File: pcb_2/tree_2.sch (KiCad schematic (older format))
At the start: 28 parts, among them J1 CONN_01x08, J2 CONN_01x08, X1 Silk_art

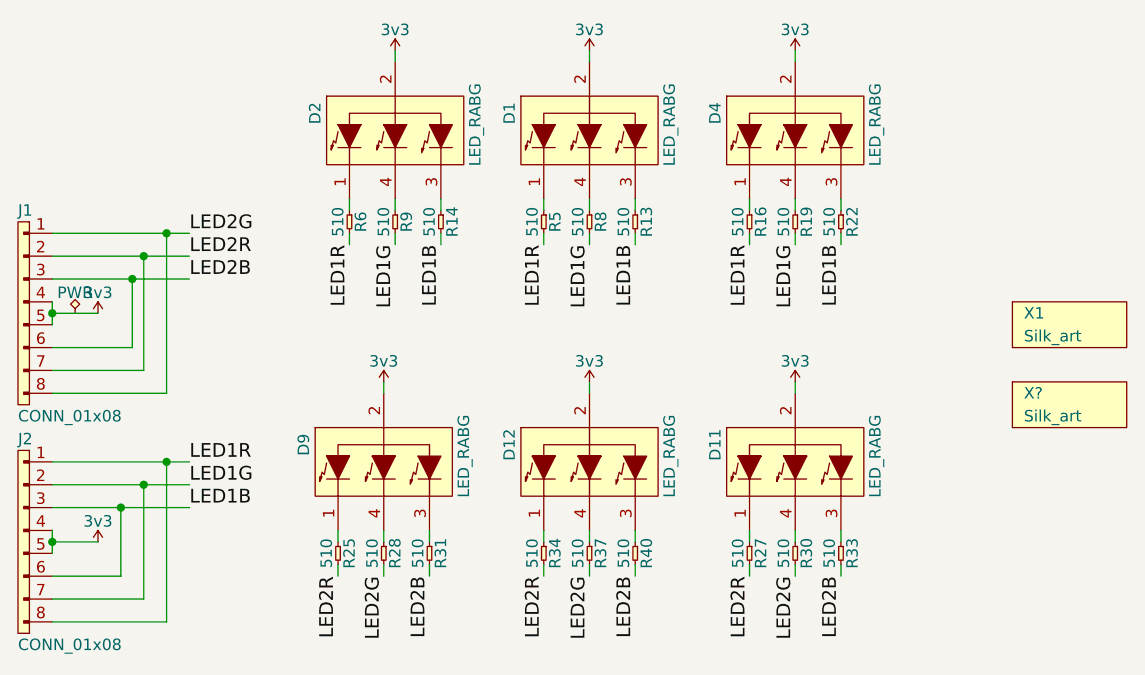
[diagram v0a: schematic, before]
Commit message: Fix circuit to account for LED currents: change resistor values, upgrade LDO regulator, use transistor array
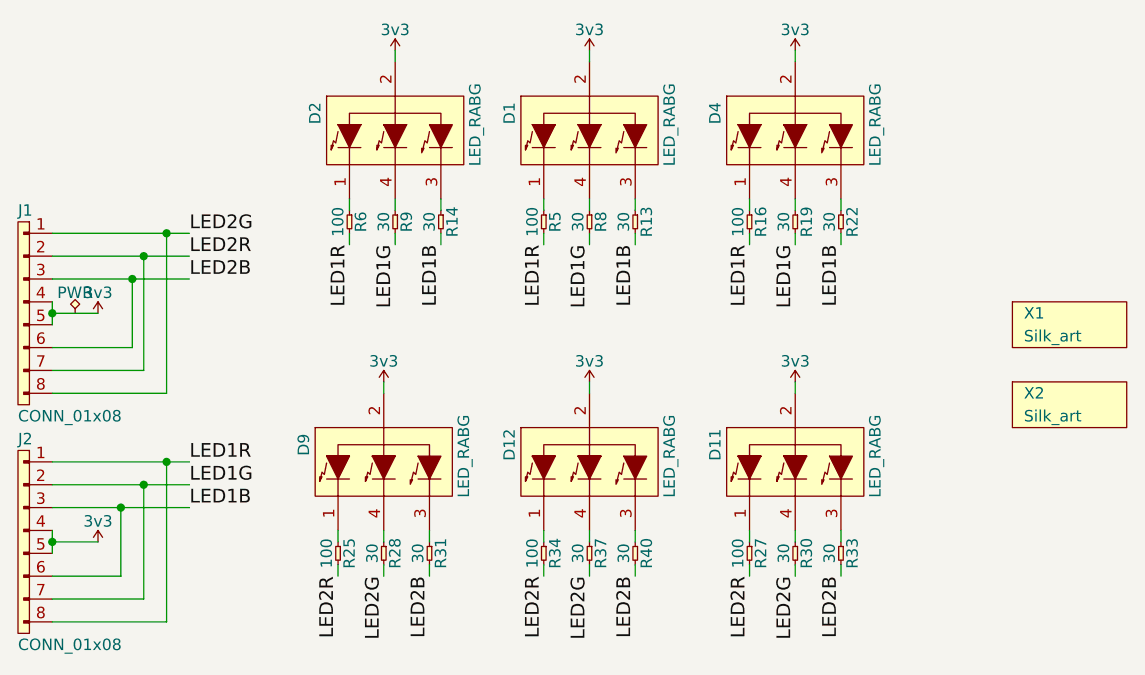
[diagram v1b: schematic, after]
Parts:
- R13, R14, R19, R22, R28, R30, R31, R33, R37, R40, R8, R9: value 510 -> 30; Farnell 9333312 -> 9333029
- R16, R25, R27, R34, R5, R6: value 510 -> 100; Farnell 9333312 -> 9332375
- gave numbers to parts that had none: 1
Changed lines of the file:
@@
 P 5750 3250
 F 0 "R31" H 5800 3300 50  0000 C CNN
-F 1 "510" H 5800 3200 50  0000 C CNN
+F 1 "30" H 5800 3200 50  0000 C CNN
 F 2 "agg:0805" H 5750 3250 50  0001 C CNN
 F 3 "" H 5750 3250 50  0001 C CNN
 F 4 "Value" H 5750 3250 60  0001 C CNN "Digikey"
-F 5 "9333312" H 5750 3250 60  0001 C CNN "Farnell"
+F 5 "9333029" H 5750 3250 60  0001 C CNN "Farnell"
 F 6 "Value" H 5750 3250 60  0001 C CNN "Fieldname"
 	1    5750 3250
@@
 P 5550 3250
 F 0 "R28" H 5600 3300 50  0000 C CNN
-F 1 "510" H 5600 3200 50  0000 C CNN
+F 1 "30" H 5600 3200 50  0000 C CNN
 F 2 "agg:0805" H 5550 3250 50  0001 C CNN
 F 3 "" H 5550 3250 50  0001 C CNN
 F 4 "Value" H 5550 3250 60  0001 C CNN "Digikey"
-F 5 "9333312" H 5550 3250 60  0001 C CNN "Farnell"
+F 5 "9333029" H 5550 3250 60  0001 C CNN "Farnell"
 F 6 "Value" H 5550 3250 60  0001 C CNN "Fieldname"
 	1    5550 3250
@@
 P 5350 3250
 F 0 "R25" H 5400 3300 50  0000 C CNN
-F 1 "510" H 5400 3200 50  0000 C CNN
+F 1 "100" H 5400 3200 50  0000 C CNN
 F 2 "agg:0805" H 5350 3250 50  0001 C CNN
 F 3 "" H 5350 3250 50  0001 C CNN
 F 4 "Value" H 5350 3250 60  0001 C CNN "Digikey"
-F 5 "9333312" H 5350 3250 60  0001 C CNN "Farnell"
+F 5 "9332375" H 5350 3250 60  0001 C CNN "Farnell"
 F 6 "Value" H 5350 3250 60  0001 C CNN "Fieldname"
 	1    5350 3250
@@
 P 7550 3250
 F 0 "R33" H 7600 3300 50  0000 C CNN
-F 1 "510" H 7600 3200 50  0000 C CNN
+F 1 "30" H 7600 3200 50  0000 C CNN
 F 2 "agg:0805" H 7550 3250 50  0001 C CNN
 F 3 "" H 7550 3250 50  0001 C CNN
 F 4 "Value" H 7550 3250 60  0001 C CNN "Digikey"
-F 5 "9333312" H 7550 3250 60  0001 C CNN "Farnell"
+F 5 "9333029" H 7550 3250 60  0001 C CNN "Farnell"
 F 6 "Value" H 7550 3250 60  0001 C CNN "Fieldname"
 	1    7550 3250
@@
 P 7350 3250
 F 0 "R30" H 7400 3300 50  0000 C CNN
-F 1 "510" H 7400 3200 50  0000 C CNN
+F 1 "30" H 7400 3200 50  0000 C CNN
 F 2 "agg:0805" H 7350 3250 50  0001 C CNN
 F 3 "" H 7350 3250 50  0001 C CNN
 F 4 "Value" H 7350 3250 60  0001 C CNN "Digikey"
-F 5 "9333312" H 7350 3250 60  0001 C CNN "Farnell"
+F 5 "9333029" H 7350 3250 60  0001 C CNN "Farnell"
 F 6 "Value" H 7350 3250 60  0001 C CNN "Fieldname"
 	1    7350 3250
@@
 P 7150 3250
 F 0 "R27" H 7200 3300 50  0000 C CNN
-F 1 "510" H 7200 3200 50  0000 C CNN
+F 1 "100" H 7200 3200 50  0000 C CNN
 F 2 "agg:0805" H 7150 3250 50  0001 C CNN
 F 3 "" H 7150 3250 50  0001 C CNN
 F 4 "Value" H 7150 3250 60  0001 C CNN "Digikey"
-F 5 "9333312" H 7150 3250 60  0001 C CNN "Farnell"
+F 5 "9332375" H 7150 3250 60  0001 C CNN "Farnell"
 F 6 "Value" H 7150 3250 60  0001 C CNN "Fieldname"
 	1    7150 3250
@@
 P 6650 3250
 F 0 "R40" H 6700 3300 50  0000 C CNN
-F 1 "510" H 6700 3200 50  0000 C CNN
+F 1 "30" H 6700 3200 50  0000 C CNN
 F 2 "agg:0805" H 6650 3250 50  0001 C CNN
 F 3 "" H 6650 3250 50  0001 C CNN
 F 4 "Value" H 6650 3250 60  0001 C CNN "Digikey"
-F 5 "9333312" H 6650 3250 60  0001 C CNN "Farnell"
+F 5 "9333029" H 6650 3250 60  0001 C CNN "Farnell"
 F 6 "Value" H 6650 3250 60  0001 C CNN "Fieldname"
 	1    6650 3250
@@
 P 6450 3250
 F 0 "R37" H 6500 3300 50  0000 C CNN
-F 1 "510" H 6500 3200 50  0000 C CNN
+F 1 "30" H 6500 3200 50  0000 C CNN
 F 2 "agg:0805" H 6450 3250 50  0001 C CNN
 F 3 "" H 6450 3250 50  0001 C CNN
 F 4 "Value" H 6450 3250 60  0001 C CNN "Digikey"
-F 5 "9333312" H 6450 3250 60  0001 C CNN "Farnell"
+F 5 "9333029" H 6450 3250 60  0001 C CNN "Farnell"
 F 6 "Value" H 6450 3250 60  0001 C CNN "Fieldname"
 	1    6450 3250
@@
 P 6250 3250
 F 0 "R34" H 6300 3300 50  0000 C CNN
-F 1 "510" H 6300 3200 50  0000 C CNN
+F 1 "100" H 6300 3200 50  0000 C CNN
 F 2 "agg:0805" H 6250 3250 50  0001 C CNN
 F 3 "" H 6250 3250 50  0001 C CNN
 F 4 "Value" H 6250 3250 60  0001 C CNN "Digikey"
-F 5 "9333312" H 6250 3250 60  0001 C CNN "Farnell"
+F 5 "9332375" H 6250 3250 60  0001 C CNN "Farnell"
 F 6 "Value" H 6250 3250 60  0001 C CNN "Fieldname"
 	1    6250 3250
@@
 P 7150 1800
 F 0 "R16" H 7200 1850 50  0000 C CNN
-F 1 "510" H 7200 1750 50  0000 C CNN
+F 1 "100" H 7200 1750 50  0000 C CNN
 F 2 "agg:0805" H 7150 1800 50  0001 C CNN
 F 3 "" H 7150 1800 50  0001 C CNN
 F 4 "Value" H 7150 1800 60  0001 C CNN "Digikey"
-F 5 "9333312" H 7150 1800 60  0001 C CNN "Farnell"
+F 5 "9332375" H 7150 1800 60  0001 C CNN "Farnell"
 F 6 "Value" H 7150 1800 60  0001 C CNN "Fieldname"
 	1    7150 1800
@@
 P 7350 1800
 F 0 "R19" H 7400 1850 50  0000 C CNN
-F 1 "510" H 7400 1750 50  0000 C CNN
+F 1 "30" H 7400 1750 50  0000 C CNN
 F 2 "agg:0805" H 7350 1800 50  0001 C CNN
 F 3 "" H 7350 1800 50  0001 C CNN
 F 4 "Value" H 7350 1800 60  0001 C CNN "Digikey"
-F 5 "9333312" H 7350 1800 60  0001 C CNN "Farnell"
+F 5 "9333029" H 7350 1800 60  0001 C CNN "Farnell"
 F 6 "Value" H 7350 1800 60  0001 C CNN "Fieldname"
 	1    7350 1800
@@
 P 7550 1800
 F 0 "R22" H 7600 1850 50  0000 C CNN
-F 1 "510" H 7600 1750 50  0000 C CNN
+F 1 "30" H 7600 1750 50  0000 C CNN
 F 2 "agg:0805" H 7550 1800 50  0001 C CNN
 F 3 "" H 7550 1800 50  0001 C CNN
 F 4 "Value" H 7550 1800 60  0001 C CNN "Digikey"
-F 5 "9333312" H 7550 1800 60  0001 C CNN "Farnell"
+F 5 "9333029" H 7550 1800 60  0001 C CNN "Farnell"
 F 6 "Value" H 7550 1800 60  0001 C CNN "Fieldname"
 	1    7550 1800
@@
 P 5400 1800
 F 0 "R6" H 5450 1850 50  0000 C CNN
-F 1 "510" H 5450 1750 50  0000 C CNN
+F 1 "100" H 5450 1750 50  0000 C CNN
 F 2 "agg:0805" H 5400 1800 50  0001 C CNN
 F 3 "" H 5400 1800 50  0001 C CNN
 F 4 "Value" H 5400 1800 60  0001 C CNN "Digikey"
-F 5 "9333312" H 5400 1800 60  0001 C CNN "Farnell"
+F 5 "9332375" H 5400 1800 60  0001 C CNN "Farnell"
 F 6 "Value" H 5400 1800 60  0001 C CNN "Fieldname"
 	1    5400 1800
@@
 P 5600 1800
 F 0 "R9" H 5650 1850 50  0000 C CNN
-F 1 "510" H 5650 1750 50  0000 C CNN
+F 1 "30" H 5650 1750 50  0000 C CNN
 F 2 "agg:0805" H 5600 1800 50  0001 C CNN
 F 3 "" H 5600 1800 50  0001 C CNN
 F 4 "Value" H 5600 1800 60  0001 C CNN "Digikey"
-F 5 "9333312" H 5600 1800 60  0001 C CNN "Farnell"
+F 5 "9333029" H 5600 1800 60  0001 C CNN "Farnell"
 F 6 "Value" H 5600 1800 60  0001 C CNN "Fieldname"
 	1    5600 1800
@@
 P 5800 1800
 F 0 "R14" H 5850 1850 50  0000 C CNN
-F 1 "510" H 5850 1750 50  0000 C CNN
+F 1 "30" H 5850 1750 50  0000 C CNN
 F 2 "agg:0805" H 5800 1800 50  0001 C CNN
 F 3 "" H 5800 1800 50  0001 C CNN
 F 4 "Value" H 5800 1800 60  0001 C CNN "Digikey"
-F 5 "9333312" H 5800 1800 60  0001 C CNN "Farnell"
+F 5 "9333029" H 5800 1800 60  0001 C CNN "Farnell"
 F 6 "Value" H 5800 1800 60  0001 C CNN "Fieldname"
 	1    5800 1800
@@
 P 6250 1800
 F 0 "R5" H 6300 1850 50  0000 C CNN
-F 1 "510" H 6300 1750 50  0000 C CNN
+F 1 "100" H 6300 1750 50  0000 C CNN
 F 2 "agg:0805" H 6250 1800 50  0001 C CNN
 F 3 "" H 6250 1800 50  0001 C CNN
 F 4 "Value" H 6250 1800 60  0001 C CNN "Digikey"
-F 5 "9333312" H 6250 1800 60  0001 C CNN "Farnell"
+F 5 "9332375" H 6250 1800 60  0001 C CNN "Farnell"
 F 6 "Value" H 6250 1800 60  0001 C CNN "Fieldname"
 	1    6250 1800
@@
 P 6450 1800
 F 0 "R8" H 6500 1850 50  0000 C CNN
-F 1 "510" H 6500 1750 50  0000 C CNN
+F 1 "30" H 6500 1750 50  0000 C CNN
 F 2 "agg:0805" H 6450 1800 50  0001 C CNN
 F 3 "" H 6450 1800 50  0001 C CNN
 F 4 "Value" H 6450 1800 60  0001 C CNN "Digikey"
-F 5 "9333312" H 6450 1800 60  0001 C CNN "Farnell"
+F 5 "9333029" H 6450 1800 60  0001 C CNN "Farnell"
 F 6 "Value" H 6450 1800 60  0001 C CNN "Fieldname"
 	1    6450 1800
@@
 P 6650 1800
 F 0 "R13" H 6700 1850 50  0000 C CNN
-F 1 "510" H 6700 1750 50  0000 C CNN
+F 1 "30" H 6700 1750 50  0000 C CNN
 F 2 "agg:0805" H 6650 1800 50  0001 C CNN
 F 3 "" H 6650 1800 50  0001 C CNN
 F 4 "Value" H 6650 1800 60  0001 C CNN "Digikey"
-F 5 "9333312" H 6650 1800 60  0001 C CNN "Farnell"
+F 5 "9333029" H 6650 1800 60  0001 C CNN "Farnell"
 F 6 "Value" H 6650 1800 60  0001 C CNN "Fieldname"
 	1    6650 1800
@@
 $EndComp
 $Comp
-L PART X?
+L PART X2
 U 1 1 5802B3F3
 P 8300 2700
-F 0 "X?" H 8350 2800 50  0000 L CNN
+F 0 "X2" H 8350 2800 50  0000 L CNN
 F 1 "Silk_art" H 8350 2700 50  0000 L CNN
 F 2 "yule:tree_silk_scaled" H 8300 2700 50  0001 C CNN

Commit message: Update LED farnell code, generate BOM
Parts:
- D1, D11, D12, D2, D4, D9: Digikey Value -> (none); Farnell 2093940 -> 1855553; Fieldname Value -> (none)
- J1, J2, R13, R14, R16, R19, R22, R25, R27, R28, R30, R31, R33, R34, R37, R40, R5, R6, R8, R9, X1, X2: Digikey Value -> (none); Fieldname Value -> (none)
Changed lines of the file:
@@
 F 2 "yule:CREE_RGB_LED" H 5500 2850 50  0001 C CNN
 F 3 "" H 5500 2850 50  0000 C CNN
-F 4 "Value" H 5550 2900 60  0001 C CNN "Digikey"
-F 5 "2093940" H 5550 2900 60  0001 C CNN "Farnell"
-F 6 "Value" H 5550 2900 60  0001 C CNN "Fieldname"
+F 4 "1855553" H 5550 2900 60  0001 C CNN "Farnell"
 	1    5550 2900
 	0    -1   -1   0
@@
 F 2 "agg:0805" H 5750 3250 50  0001 C CNN
 F 3 "" H 5750 3250 50  0001 C CNN
-F 4 "Value" H 5750 3250 60  0001 C CNN "Digikey"
-F 5 "9333029" H 5750 3250 60  0001 C CNN "Farnell"
-F 6 "Value" H 5750 3250 60  0001 C CNN "Fieldname"
+F 4 "9333029" H 5750 3250 60  0001 C CNN "Farnell"
 	1    5750 3250
 	0    1    1    0
@@
 F 2 "agg:0805" H 5550 3250 50  0001 C CNN
 F 3 "" H 5550 3250 50  0001 C CNN
-F 4 "Value" H 5550 3250 60  0001 C CNN "Digikey"
-F 5 "9333029" H 5550 3250 60  0001 C CNN "Farnell"
-F 6 "Value" H 5550 3250 60  0001 C CNN "Fieldname"
+F 4 "9333029" H 5550 3250 60  0001 C CNN "Farnell"
 	1    5550 3250
 	0    1    1    0
@@
 F 2 "agg:0805" H 5350 3250 50  0001 C CNN
 F 3 "" H 5350 3250 50  0001 C CNN
-F 4 "Value" H 5350 3250 60  0001 C CNN "Digikey"
-F 5 "9332375" H 5350 3250 60  0001 C CNN "Farnell"
-F 6 "Value" H 5350 3250 60  0001 C CNN "Fieldname"
+F 4 "9332375" H 5350 3250 60  0001 C CNN "Farnell"
 	1    5350 3250
 	0    1    1    0
@@
 F 2 "yule:CREE_RGB_LED" H 7300 2850 50  0001 C CNN
 F 3 "" H 7300 2850 50  0000 C CNN
-F 4 "Value" H 7350 2900 60  0001 C CNN "Digikey"
-F 5 "2093940" H 7350 2900 60  0001 C CNN "Farnell"
-F 6 "Value" H 7350 2900 60  0001 C CNN "Fieldname"
+F 4 "1855553" H 7350 2900 60  0001 C CNN "Farnell"
 	1    7350 2900
 	0    -1   -1   0
@@
 F 2 "agg:0805" H 7550 3250 50  0001 C CNN
 F 3 "" H 7550 3250 50  0001 C CNN
-F 4 "Value" H 7550 3250 60  0001 C CNN "Digikey"
-F 5 "9333029" H 7550 3250 60  0001 C CNN "Farnell"
-F 6 "Value" H 7550 3250 60  0001 C CNN "Fieldname"
+F 4 "9333029" H 7550 3250 60  0001 C CNN "Farnell"
 	1    7550 3250
 	0    1    1    0
@@
 F 2 "agg:0805" H 7350 3250 50  0001 C CNN
 F 3 "" H 7350 3250 50  0001 C CNN
-F 4 "Value" H 7350 3250 60  0001 C CNN "Digikey"
-F 5 "9333029" H 7350 3250 60  0001 C CNN "Farnell"
-F 6 "Value" H 7350 3250 60  0001 C CNN "Fieldname"
+F 4 "9333029" H 7350 3250 60  0001 C CNN "Farnell"
 	1    7350 3250
 	0    1    1    0
@@
 F 2 "agg:0805" H 7150 3250 50  0001 C CNN
 F 3 "" H 7150 3250 50  0001 C CNN
-F 4 "Value" H 7150 3250 60  0001 C CNN "Digikey"
-F 5 "9332375" H 7150 3250 60  0001 C CNN "Farnell"
-F 6 "Value" H 7150 3250 60  0001 C CNN "Fieldname"
+F 4 "9332375" H 7150 3250 60  0001 C CNN "Farnell"
 	1    7150 3250
 	0    1    1    0
@@
 F 2 "yule:CREE_RGB_LED" H 6400 2850 50  0001 C CNN
 F 3 "" H 6400 2850 50  0000 C CNN
-F 4 "Value" H 6450 2900 60  0001 C CNN "Digikey"
-F 5 "2093940" H 6450 2900 60  0001 C CNN "Farnell"
-F 6 "Value" H 6450 2900 60  0001 C CNN "Fieldname"
+F 4 "1855553" H 6450 2900 60  0001 C CNN "Farnell"
 	1    6450 2900
 	0    -1   -1   0
@@
 F 2 "agg:0805" H 6650 3250 50  0001 C CNN
 F 3 "" H 6650 3250 50  0001 C CNN
-F 4 "Value" H 6650 3250 60  0001 C CNN "Digikey"
-F 5 "9333029" H 6650 3250 60  0001 C CNN "Farnell"
-F 6 "Value" H 6650 3250 60  0001 C CNN "Fieldname"
+F 4 "9333029" H 6650 3250 60  0001 C CNN "Farnell"
 	1    6650 3250
 	0    1    1    0
@@
 F 2 "agg:0805" H 6450 3250 50  0001 C CNN
 F 3 "" H 6450 3250 50  0001 C CNN
-F 4 "Value" H 6450 3250 60  0001 C CNN "Digikey"
-F 5 "9333029" H 6450 3250 60  0001 C CNN "Farnell"
-F 6 "Value" H 6450 3250 60  0001 C CNN "Fieldname"
+F 4 "9333029" H 6450 3250 60  0001 C CNN "Farnell"
 	1    6450 3250
 	0    1    1    0
@@
 F 2 "agg:0805" H 6250 3250 50  0001 C CNN
 F 3 "" H 6250 3250 50  0001 C CNN
-F 4 "Value" H 6250 3250 60  0001 C CNN "Digikey"
-F 5 "9332375" H 6250 3250 60  0001 C CNN "Farnell"
-F 6 "Value" H 6250 3250 60  0001 C CNN "Fieldname"
+F 4 "9332375" H 6250 3250 60  0001 C CNN "Farnell"
 	1    6250 3250
 	0    1    1    0
@@
 F 2 "agg:0805" H 7150 1800 50  0001 C CNN
 F 3 "" H 7150 1800 50  0001 C CNN
-F 4 "Value" H 7150 1800 60  0001 C CNN "Digikey"
-F 5 "9332375" H 7150 1800 60  0001 C CNN "Farnell"
-F 6 "Value" H 7150 1800 60  0001 C CNN "Fieldname"
+F 4 "9332375" H 7150 1800 60  0001 C CNN "Farnell"
 	1    7150 1800
 	0    1    1    0
@@
 F 2 "agg:0805" H 7350 1800 50  0001 C CNN
 F 3 "" H 7350 1800 50  0001 C CNN
-F 4 "Value" H 7350 1800 60  0001 C CNN "Digikey"
-F 5 "9333029" H 7350 1800 60  0001 C CNN "Farnell"
-F 6 "Value" H 7350 1800 60  0001 C CNN "Fieldname"
+F 4 "9333029" H 7350 1800 60  0001 C CNN "Farnell"
 	1    7350 1800
 	0    1    1    0
@@
 F 2 "agg:0805" H 7550 1800 50  0001 C CNN
 F 3 "" H 7550 1800 50  0001 C CNN
-F 4 "Value" H 7550 1800 60  0001 C CNN "Digikey"
-F 5 "9333029" H 7550 1800 60  0001 C CNN "Farnell"
-F 6 "Value" H 7550 1800 60  0001 C CNN "Fieldname"
+F 4 "9333029" H 7550 1800 60  0001 C CNN "Farnell"
 	1    7550 1800
 	0    1    1    0
@@
 F 2 "yule:CREE_RGB_LED" H 7300 1400 50  0001 C CNN
 F 3 "" H 7300 1400 50  0000 C CNN
-F 4 "Value" H 7350 1450 60  0001 C CNN "Digikey"
-F 5 "2093940" H 7350 1450 60  0001 C CNN "Farnell"
-F 6 "Value" H 7350 1450 60  0001 C CNN "Fieldname"
+F 4 "1855553" H 7350 1450 60  0001 C CNN "Farnell"
 	1    7350 1450
 	0    -1   -1   0
@@
 F 2 "agg:0805" H 5400 1800 50  0001 C CNN
 F 3 "" H 5400 1800 50  0001 C CNN
-F 4 "Value" H 5400 1800 60  0001 C CNN "Digikey"
-F 5 "9332375" H 5400 1800 60  0001 C CNN "Farnell"
-F 6 "Value" H 5400 1800 60  0001 C CNN "Fieldname"
+F 4 "9332375" H 5400 1800 60  0001 C CNN "Farnell"
 	1    5400 1800
 	0    1    1    0
@@
 F 2 "agg:0805" H 5600 1800 50  0001 C CNN
 F 3 "" H 5600 1800 50  0001 C CNN
-F 4 "Value" H 5600 1800 60  0001 C CNN "Digikey"
-F 5 "9333029" H 5600 1800 60  0001 C CNN "Farnell"
-F 6 "Value" H 5600 1800 60  0001 C CNN "Fieldname"
+F 4 "9333029" H 5600 1800 60  0001 C CNN "Farnell"
 	1    5600 1800
 	0    1    1    0
@@
 F 2 "agg:0805" H 5800 1800 50  0001 C CNN
 F 3 "" H 5800 1800 50  0001 C CNN
-F 4 "Value" H 5800 1800 60  0001 C CNN "Digikey"
-F 5 "9333029" H 5800 1800 60  0001 C CNN "Farnell"
-F 6 "Value" H 5800 1800 60  0001 C CNN "Fieldname"
+F 4 "9333029" H 5800 1800 60  0001 C CNN "Farnell"
 	1    5800 1800
 	0    1    1    0
@@
 F 2 "yule:CREE_RGB_LED" H 5550 1400 50  0001 C CNN
 F 3 "" H 5550 1400 50  0000 C CNN
-F 4 "Value" H 5600 1450 60  0001 C CNN "Digikey"
-F 5 "2093940" H 5600 1450 60  0001 C CNN "Farnell"
-F 6 "Value" H 5600 1450 60  0001 C CNN "Fieldname"
+F 4 "1855553" H 5600 1450 60  0001 C CNN "Farnell"
 	1    5600 1450
 	0    -1   -1   0
@@
 F 2 "agg:0805" H 6250 1800 50  0001 C CNN
 F 3 "" H 6250 1800 50  0001 C CNN
-F 4 "Value" H 6250 1800 60  0001 C CNN "Digikey"
-F 5 "9332375" H 6250 1800 60  0001 C CNN "Farnell"
-F 6 "Value" H 6250 1800 60  0001 C CNN "Fieldname"
+F 4 "9332375" H 6250 1800 60  0001 C CNN "Farnell"
 	1    6250 1800
 	0    1    1    0
@@
 F 2 "agg:0805" H 6450 1800 50  0001 C CNN
 F 3 "" H 6450 1800 50  0001 C CNN
-F 4 "Value" H 6450 1800 60  0001 C CNN "Digikey"
-F 5 "9333029" H 6450 1800 60  0001 C CNN "Farnell"
-F 6 "Value" H 6450 1800 60  0001 C CNN "Fieldname"
+F 4 "9333029" H 6450 1800 60  0001 C CNN "Farnell"
 	1    6450 1800
 	0    1    1    0
@@
 F 2 "agg:0805" H 6650 1800 50  0001 C CNN
 F 3 "" H 6650 1800 50  0001 C CNN
-F 4 "Value" H 6650 1800 60  0001 C CNN "Digikey"
-F 5 "9333029" H 6650 1800 60  0001 C CNN "Farnell"
-F 6 "Value" H 6650 1800 60  0001 C CNN "Fieldname"
+F 4 "9333029" H 6650 1800 60  0001 C CNN "Farnell"
 	1    6650 1800
 	0    1    1    0
@@
 F 2 "yule:CREE_RGB_LED" H 6400 1400 50  0001 C CNN
 F 3 "http://www.farnell.com/datasheets/1965387.pdf" H 6400 1400 50  0001 C CNN
-F 4 "Value" H 6450 1450 60  0001 C CNN "Digikey"
-F 5 "2093940" H 6450 1450 60  0001 C CNN "Farnell"
-F 6 "Value" H 6450 1450 60  0001 C CNN "Fieldname"
+F 4 "1855553" H 6450 1450 60  0001 C CNN "Farnell"
 	1    6450 1450
 	0    -1   -1   0
@@
 F 2 "yule:Interboard" H 4000 1900 50  0001 C CNN
 F 3 "" H 4000 1900 50  0001 C CNN
-F 4 "Value" H 4000 1900 60  0001 C CNN "Digikey"
-F 5 "Value" H 4000 1900 60  0001 C CNN "Farnell"
-F 6 "Value" H 4000 1900 60  0001 C CNN "Fieldname"
+F 4 "Value" H 4000 1900 60  0001 C CNN "Farnell"
 	1    4000 1900
 	1    0    0    -1
@@
 F 2 "yule:Interboard" H 4000 2900 50  0001 C CNN
 F 3 "" H 4000 2900 50  0001 C CNN
-F 4 "Value" H 4000 2900 60  0001 C CNN "Digikey"
-F 5 "Value" H 4000 2900 60  0001 C CNN "Farnell"
-F 6 "Value" H 4000 2900 60  0001 C CNN "Fieldname"
+F 4 "Value" H 4000 2900 60  0001 C CNN "Farnell"
 	1    4000 2900
 	1    0    0    -1
@@
 F 2 "yule:tree_silk_scaled" H 8300 2350 50  0001 C CNN
 F 3 "" H 8300 2350 50  0001 C CNN
-F 4 "Value" H 8300 2350 60  0001 C CNN "Digikey"
-F 5 "Value" H 8300 2350 60  0001 C CNN "Farnell"
-F 6 "Value" H 8300 2350 60  0001 C CNN "Fieldname"
+F 4 "Value" H 8300 2350 60  0001 C CNN "Farnell"
 	1    8300 2350
 	1    0    0    -1
@@
 F 2 "yule:tree_silk_scaled" H 8300 2700 50  0001 C CNN
 F 3 "" H 8300 2700 50  0001 C CNN
-F 4 "Value" H 8300 2700 60  0001 C CNN "Digikey"
-F 5 "Value" H 8300 2700 60  0001 C CNN "Farnell"
-F 6 "Value" H 8300 2700 60  0001 C CNN "Fieldname"
+F 4 "Value" H 8300 2700 60  0001 C CNN "Farnell"
 	1    8300 2700
 	1    0    0    -1
